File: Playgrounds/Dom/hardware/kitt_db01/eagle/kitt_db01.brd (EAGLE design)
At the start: 51.5 x 31 mm, 16 parts, among them Q1 [MMBF170], U1 ADNS-3080, X1 RESON

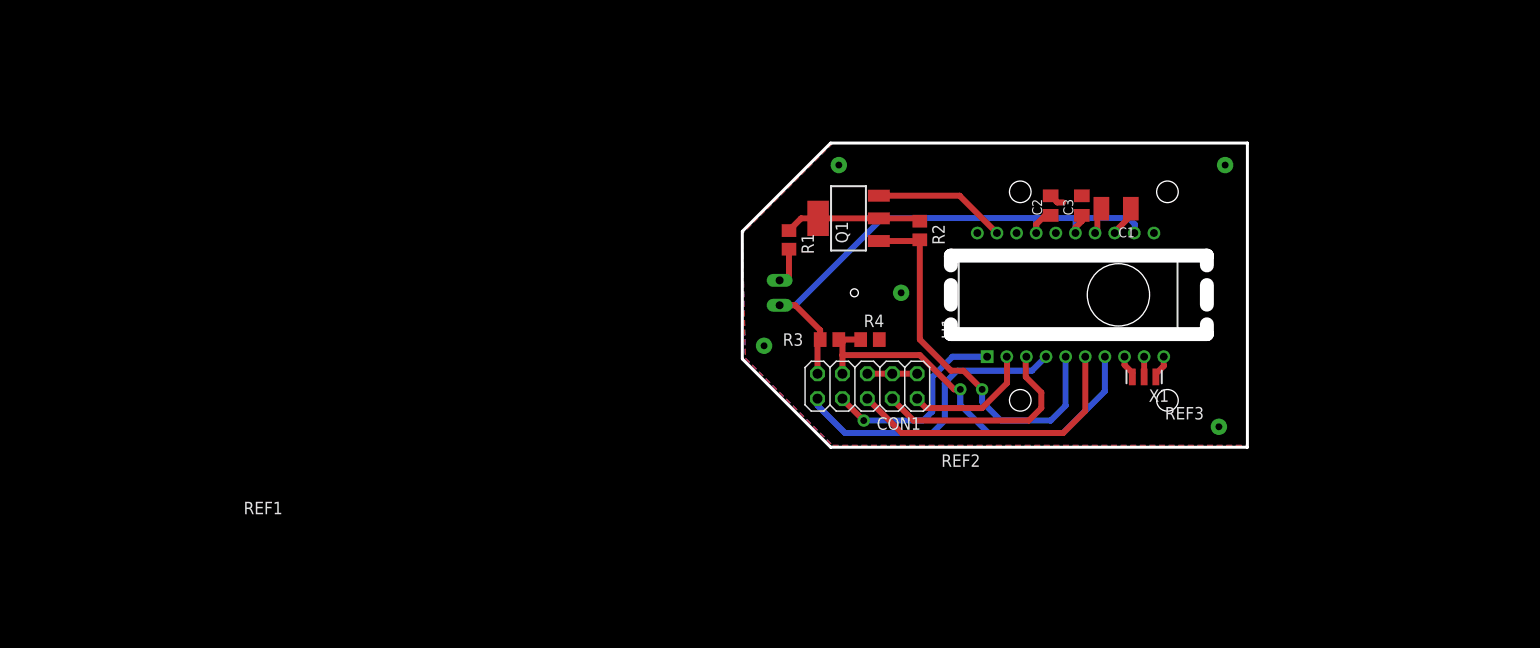
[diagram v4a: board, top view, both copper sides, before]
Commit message: general improvements for DB01  - optimized the connector layout in regards to the MB01  - as there is more board area, an optional 3V3 LDO was added  - now featuring a power indicator  - added an (optional) input for manual LED control
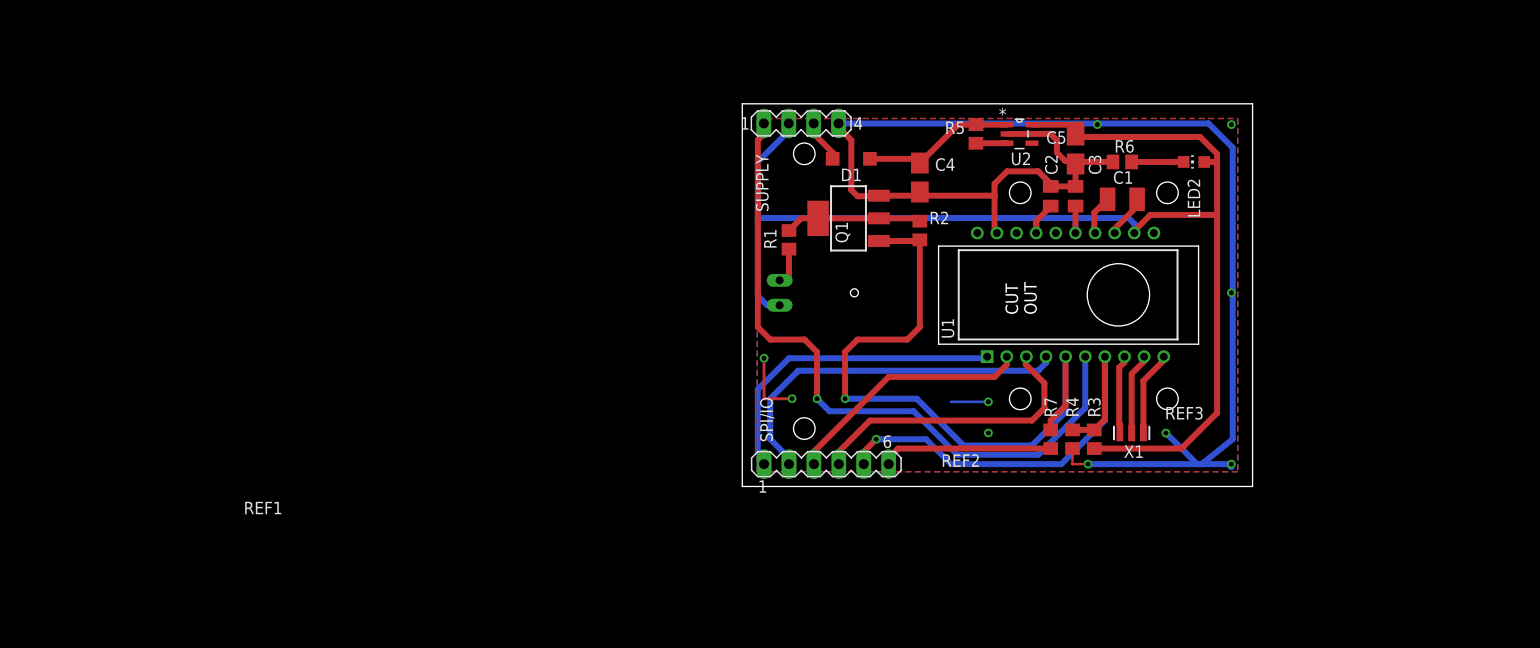
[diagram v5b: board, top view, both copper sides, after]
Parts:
- removed CON1: (no value), pinhead:2X05
- added C4, C5: 1uF, rcl:A/3216-18W
- added D1: MBR0520LT, diode:SOD123
- added LED2: POWER, led:CHIP-LED0805
- added R5, R7: [0R], rcl:R0805
- added R6: [PPR], rcl:R0805
- added SPI/IO: (no value), con-lstb:MA06-1
- added SUPPLY: (no value), con-lstb:MA04-1
- added U2: MIC5205-3.3YM5TR, kitt.ic:SOT95P280X130-5N
- moved R3 28.8 mm to (102.9, 43.8), turned to 90 degrees
- moved R4 23.0 mm to (100.6, 43.8), turned to 270 degrees
- moved X1 5.85 mm to (106.7, 44.4)
- moved C1 1.14 mm to (105.7, 68.3)
- moved C3 1.14 mm to (101.0, 68.6)
- moved C2 0.95 mm to (98.4, 68.6)
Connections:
- new net !LEDCTRL: R7.2, SPI/IO.6
- new net +5V: D1.A, SUPPLY.3
- new net N$10: R5.2, U2.3
- new net N$11: LED2.C, R6.1
- new net N$9: C4.+, D1.C, R5.1, U2.1
- net !CS: now also SPI/IO.1; no longer CON1.3
- net !PD: now also SPI/IO.5; no longer CON1.4
- net +3V3: now also C5.+, LED2.A, SUPPLY.2, U2.5; no longer CON1.2
- net GND: now also C4.-, C5.-, R6.2, SUPPLY.4, U2.2; no longer CON1.10, CON1.6, CON1.8
- net MISO: now also SPI/IO.3; no longer CON1.9
- net MOSI: now also SPI/IO.2; no longer CON1.1
- net N$4: now also R7.1
- net RST: now also SUPPLY.1; no longer CON1.5
- net SCLK: now also SPI/IO.4; no longer CON1.7
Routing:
- net GND: track 20.3 -> 162.1 mm, vias 5 -> 10
- net +3V3: track 60.2 -> 143.1 mm
- net RST: track 30.1 -> 69.8 mm, vias 0 -> 1
- net N$4: track 39.0 -> 66.1 mm
- net !LEDCTRL: track 0.00 -> 17.5 mm
- net N$9: track 0.00 -> 16.4 mm
- net MISO: track 13.4 -> 25.7 mm
- net !CS: track 20.5 -> 32.6 mm, vias 1 -> 0
- net SCLK: track 22.6 -> 31.0 mm
- net MOSI: track 30.8 -> 38.0 mm
- net N$1: track 2.07 -> 8.31 mm
- net N$3: track 2.40 -> 8.64 mm
- net N$2: track 2.40 -> 8.03 mm
- net N$11: track 0.00 -> 5.30 mm
- net +5V: track 0.00 -> 4.41 mm
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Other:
- board size 51.5 x 31 mm -> 52 x 39 mm
- board text added: "CUT OUT"

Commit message: updated board dimensions and LED/ADNS3080 placement
still need to figure out the arduino pin situration tough prior to
routing and placement
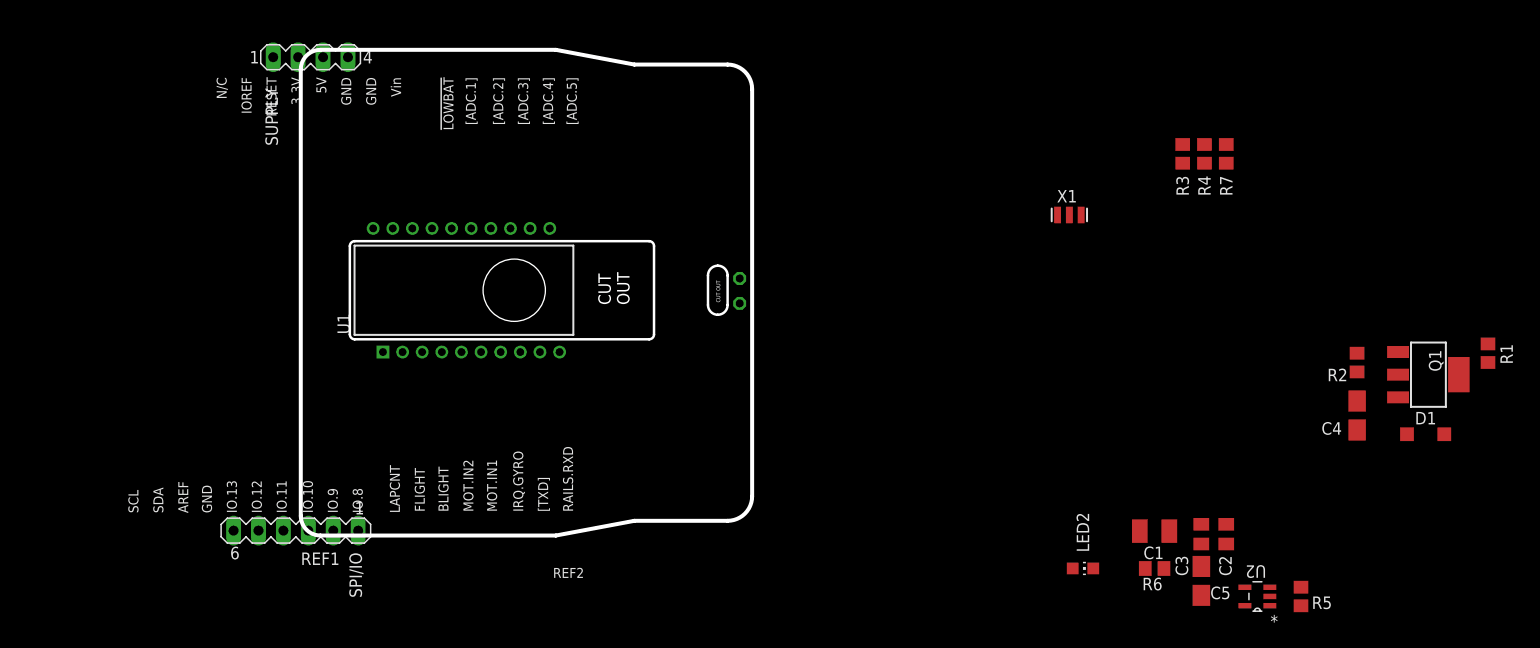
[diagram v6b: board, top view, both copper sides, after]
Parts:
- removed REF3: SC-8000-C, scaleauto:SC-8000-C
- LED1: device led:Q62902-B155 -> led:LED5MM
- REF1: value SC-8000-A -> REF.KITT-DB01; device scaleauto:SC-8000-A -> kitt.refs:REF_KITT-DB01
- REF2: value SC-8000-B -> REF_GC-BBV2.0; device scaleauto:SC-8000-B -> kitt.con:REF_GHOSTCAR
- moved REF2 79.6 mm to (26.8, 58.0), turned to 180 degrees
- moved R1 72.2 mm to (143.0, 52.6), turned to 90 degrees
- moved D1 64.9 mm to (136.6, 44.3), turned to 0 degrees
- moved U1 61.6 mm to (38.5, 59.0)
- moved Q1 61.2 mm to (136.9, 50.4), turned to 270 degrees
- moved R5 57.6 mm to (123.9, 27.8), turned to 90 degrees
- moved SPI/IO 54.5 mm to (21.5, 34.5), turned to 180 degrees
- moved U2 53.0 mm to (119.5, 27.8), turned to 180 degrees
- moved C4 50.7 mm to (129.7, 46.2), turned to 270 degrees
- moved SUPPLY 50.5 mm to (23.0, 82.8)
- moved R2 46.6 mm to (129.7, 51.6), turned to 90 degrees
- moved C5 45.8 mm to (113.8, 29.4), turned to 270 degrees
- moved LED2 42.9 mm to (101.7, 30.6), turned to 270 degrees
- moved R6 41.6 mm to (109.0, 30.6), turned to 0 degrees
- moved C2 38.8 mm to (116.3, 34.1), turned to 270 degrees
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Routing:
- net GND: track 162.1 -> 0.00 mm, vias 10 -> 0
- net +3V3: track 143.1 -> 0.00 mm
- net RST: track 69.8 -> 0.00 mm, vias 1 -> 0
- net N$4: track 66.1 -> 0.00 mm, vias 1 -> 0
- net !PD: track 45.9 -> 0.00 mm, vias 1 -> 0
- net MOSI: track 38.0 -> 0.00 mm
- net !CS: track 32.6 -> 0.00 mm
- net SCLK: track 31.0 -> 0.00 mm
- net MISO: track 25.7 -> 0.00 mm
- net !LEDCTRL: track 17.5 -> 0.00 mm
- net N$9: track 16.4 -> 0.00 mm
- net N$7: track 14.0 -> 0.00 mm
- net N$3: track 8.64 -> 0.00 mm
- net N$1: track 8.31 -> 0.00 mm
- net N$2: track 8.03 -> 0.00 mm
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- removed copper zone on layer 1, net GND
- removed copper zone on layer 16, net GND
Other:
- board size 52 x 39 mm -> 46 x 49.5 mm

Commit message: updated the placement of the pinheaders and such
beginning now with routing
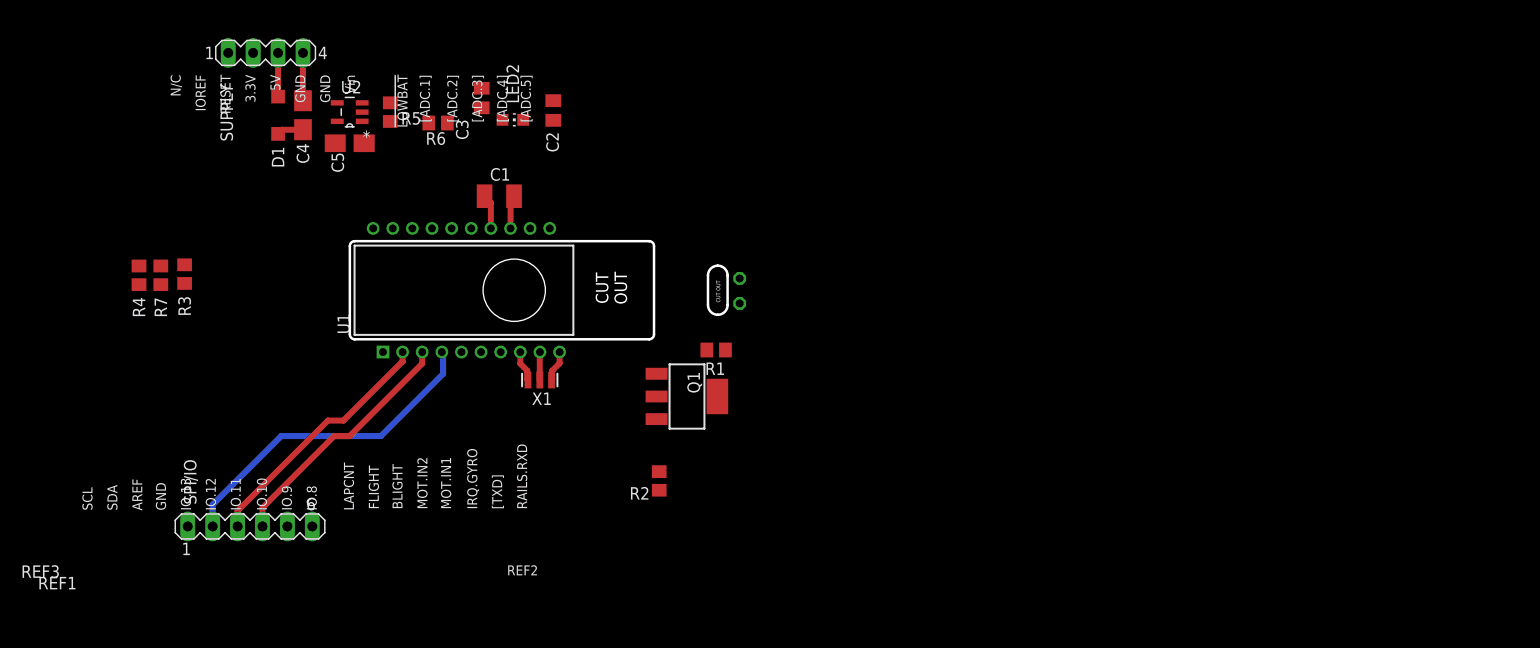
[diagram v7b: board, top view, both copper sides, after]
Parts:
- added REF3: REF.KITT-MB01, kitt.refs:REF_KITT_MB01
- moved D1 121.4 mm to (19.7, 76.8), turned to 90 degrees
- moved C4 111.7 mm to (22.2, 76.8)
- moved R4 109.3 mm to (5.51, 60.5)
- moved R7 109.3 mm to (7.74, 60.5)
- moved R5 105.1 mm to (31.1, 77.2)
- moved U2 104.9 mm to (27.0, 77.2)
- moved R3 102.5 mm to (10.2, 60.6)
- moved C5 97.6 mm to (27.0, 74.0), turned to 180 degrees
- moved R6 86.0 mm to (36.0, 76.0)
- moved C3 85.8 mm to (40.4, 78.6)
- moved C2 81.0 mm to (47.7, 77.3)
- moved R1 78.7 mm to (64.3, 52.9), turned to 0 degrees
- moved Q1 75.6 mm to (61.4, 48.2)
- moved C1 75.0 mm to (42.2, 68.6), turned to 180 degrees
- moved LED2 73.9 mm to (43.6, 76.4)
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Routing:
- net MOSI: track 0.00 -> 33.5 mm
- net MISO: track 0.00 -> 25.7 mm
- net SCLK: track 0.00 -> 25.4 mm
- net GND: track 0.00 -> 4.88 mm
- net +5V: track 0.00 -> 4.45 mm
- net N$6: track 0.00 -> 3.55 mm
- net N$5: track 0.00 -> 3.43 mm
- net N$3: track 0.00 -> 3.19 mm
- net N$2: track 0.00 -> 3.18 mm
- net N$1: track 0.00 -> 2.86 mm
- net N$9: track 0.00 -> 2.72 mm
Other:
- board size 46 x 49.5 mm -> 38.5 x 10 mm

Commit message: placement and basic routing done for db01
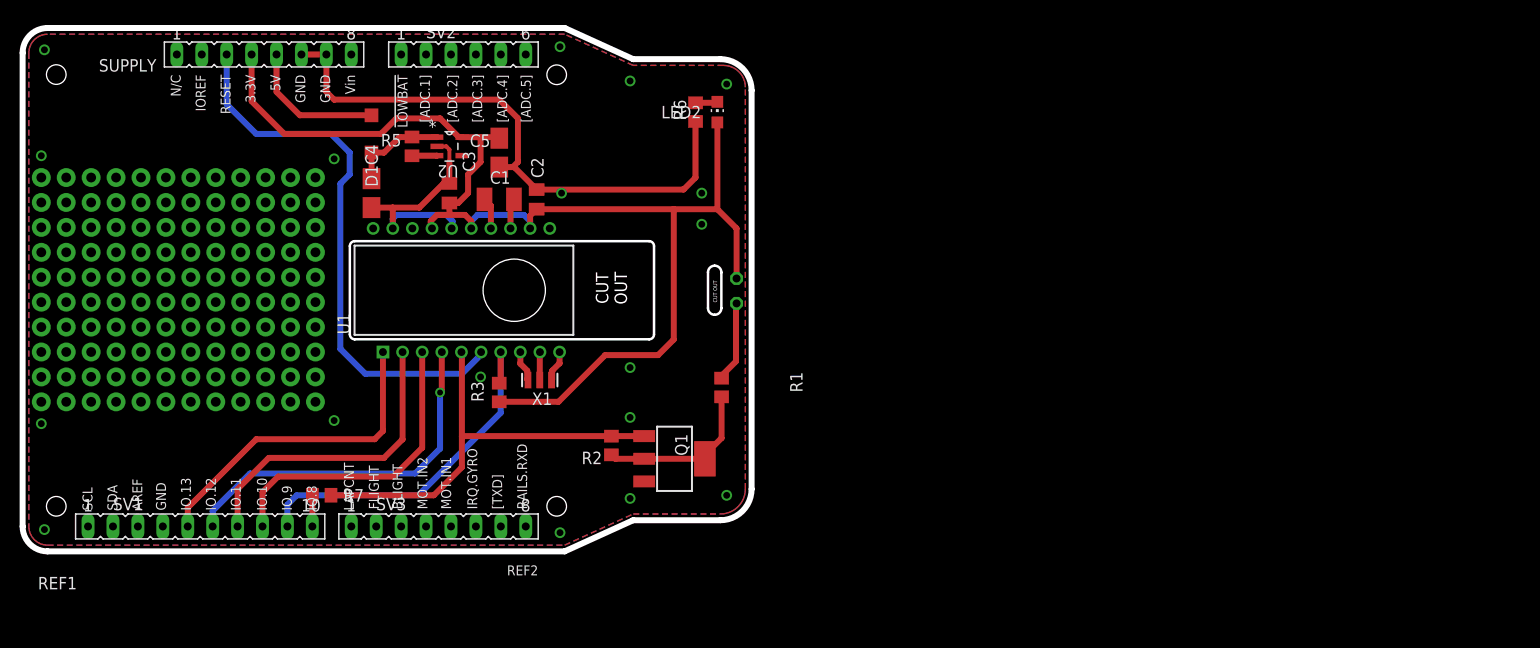
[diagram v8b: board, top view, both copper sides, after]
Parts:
- removed R4: [PPR], rcl:R0805
- removed REF3: REF.KITT-MB01, kitt.refs:REF_KITT_MB01
- removed SPI/IO: (no value), con-lstb:MA06-1
- added SV1: (no value), con-lsta:FE10
- added SV2: (no value), con-lsta:FE06
- added SV3: (no value), con-lsta:FE08
- SUPPLY: device con-lstb:MA04-1 -> con-lsta:FE08
- moved R3 34.3 mm to (42.2, 48.6), turned to 90 degrees
- moved R7 27.8 mm to (24.1, 38.1), turned to 180 degrees
- moved R6 26.3 mm to (62.2, 77.2), turned to 270 degrees
- moved LED2 20.9 mm to (64.5, 77.2), turned to 0 degrees
- moved C5 15.3 mm to (42.2, 73.0), turned to 90 degrees
- moved U2 10.7 mm to (37.1, 73.7), turned to 0 degrees
- moved C4 10.6 mm to (29.2, 68.9), turned to 90 degrees
- moved C3 10.2 mm to (37.1, 68.9), turned to 90 degrees
- moved D1 9.71 mm to (29.2, 74.9)
- moved C2 9.21 mm to (46.0, 68.3), turned to 90 degrees
- moved Q1 6.48 mm to (60.1, 41.8)
- moved R2 6.07 mm to (53.7, 43.2)
- moved R5 4.14 mm to (33.3, 73.7), turned to 270 degrees
- moved R1 3.86 mm to (64.9, 49.1), turned to 90 degrees
- moved LED1 0.32 mm to (66.4, 58.9)
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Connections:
- net !CS: now also SV1.5; no longer SPI/IO.1
- net !LEDCTRL: now also SV1.10; no longer SPI/IO.6
- net !PD: now also SV1.9; no longer R4.1, SPI/IO.5
- net +3V3: now also SUPPLY.4; no longer SUPPLY.2
- net +5V: now also SUPPLY.5; no longer SUPPLY.3
- net GND: now also SUPPLY.6, SUPPLY.7, SV1.4; no longer R4.2, SUPPLY.4
- net MISO: now also SV1.7; no longer SPI/IO.3
- net MOSI: now also SV1.6; no longer SPI/IO.2
- net RST: now also SUPPLY.3; no longer SUPPLY.1
- net SCLK: now also SV1.8; no longer SPI/IO.4
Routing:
- net +3V3: track 0.00 -> 128.3 mm
- net GND: track 4.88 -> 83.6 mm, vias 0 -> 18
- net RST: track 0.00 -> 56.5 mm
- net N$4: track 0.00 -> 44.9 mm
- net !PD: track 0.00 -> 37.3 mm
- net !CS: track 0.00 -> 33.1 mm
- net N$7: track 0.00 -> 16.7 mm
- net +5V: track 4.45 -> 14.5 mm
- net N$8: track 0.00 -> 8.23 mm
- net N$9: track 2.72 -> 9.99 mm
- net SCLK: track 25.4 -> 31.4 mm
- net MISO: track 25.7 -> 31.6 mm
- net MOSI: track 33.5 -> 37.3 mm, vias 0 -> 1
- net !LEDCTRL: track 0.00 -> 3.18 mm
- net N$10: track 0.00 -> 2.55 mm
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- added copper zone on layer 1, net GND
- added copper zone on layer 16, net GND
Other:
- board size 38.5 x 10 mm -> 74.3 x 53.3 mm
- board text added: "The Prototyping Area is here because: - it enables quick bodgejobs - it uses up real estate which would be wasted otherwise"
